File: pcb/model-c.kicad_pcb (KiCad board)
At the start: 2 copper layers, 82 x 144.9 mm, 115 parts, among them IC1 HTK16K33, IC2 HTK16K33, J1 Batt, J2 Conn_01x02_Socket, SW1 SW_SPST, SW10 SW_SPST, SW11 SW_SPST, SW12 SW_SPST, SW13 SW_SPST, SW14 SW_SPST, SW15 SW_SPST, SW16 SW_SPST, SW17 SW_SPST, SW18 SW_SPST, SW19 SW_SPST, SW2 SW_SPST, SW20 SW_SPDT, SW3 SW_SPST, SW4 SW_SPST, SW5 SW_SPST, SW6 SW_SPST, SW7 SW_SPST, SW8 SW_SPST, SW9 SW_SPST, U1 W25Q16JVUXIQ, U2 14seg, U3 RP2040, U4 MCP73831-2-OT, U5 XC9140, U6 14seg, Y1 12MHz

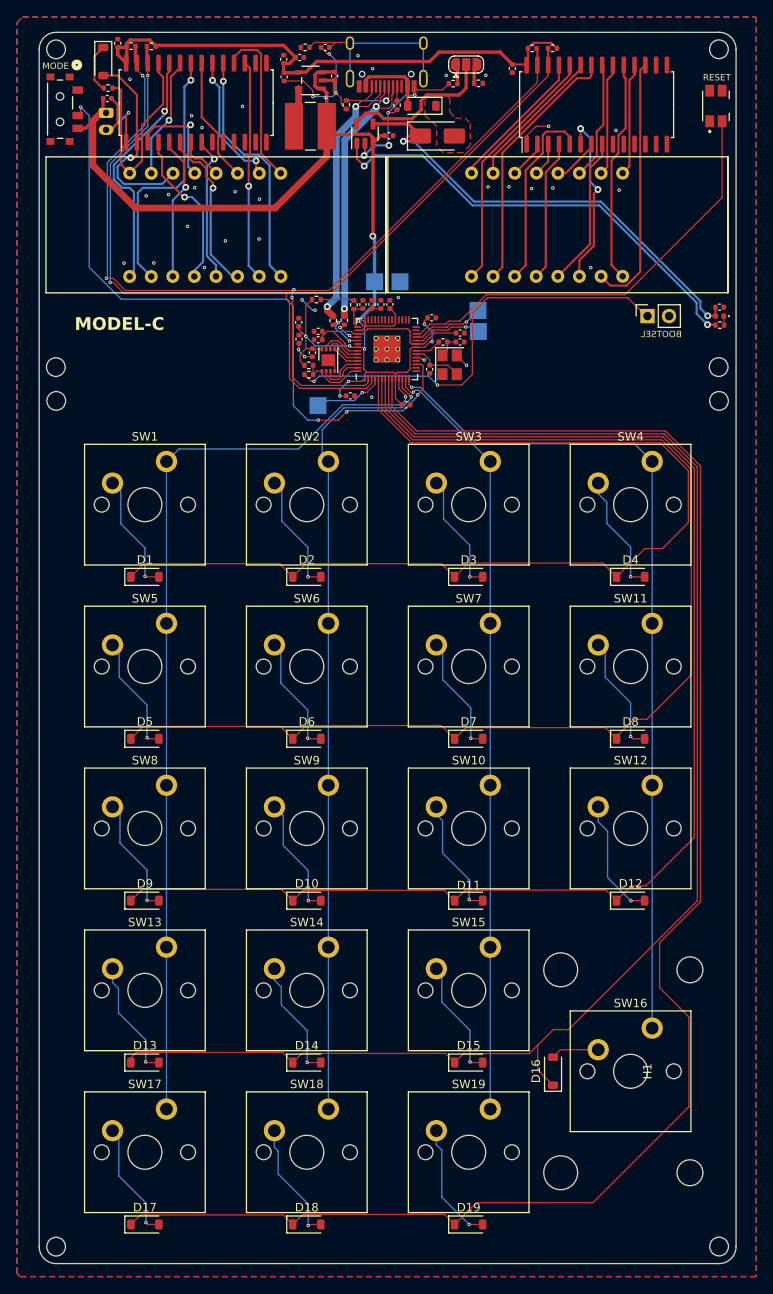
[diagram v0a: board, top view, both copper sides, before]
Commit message: fixed power switch, mode button, updated readme, panelized, and added much better styling
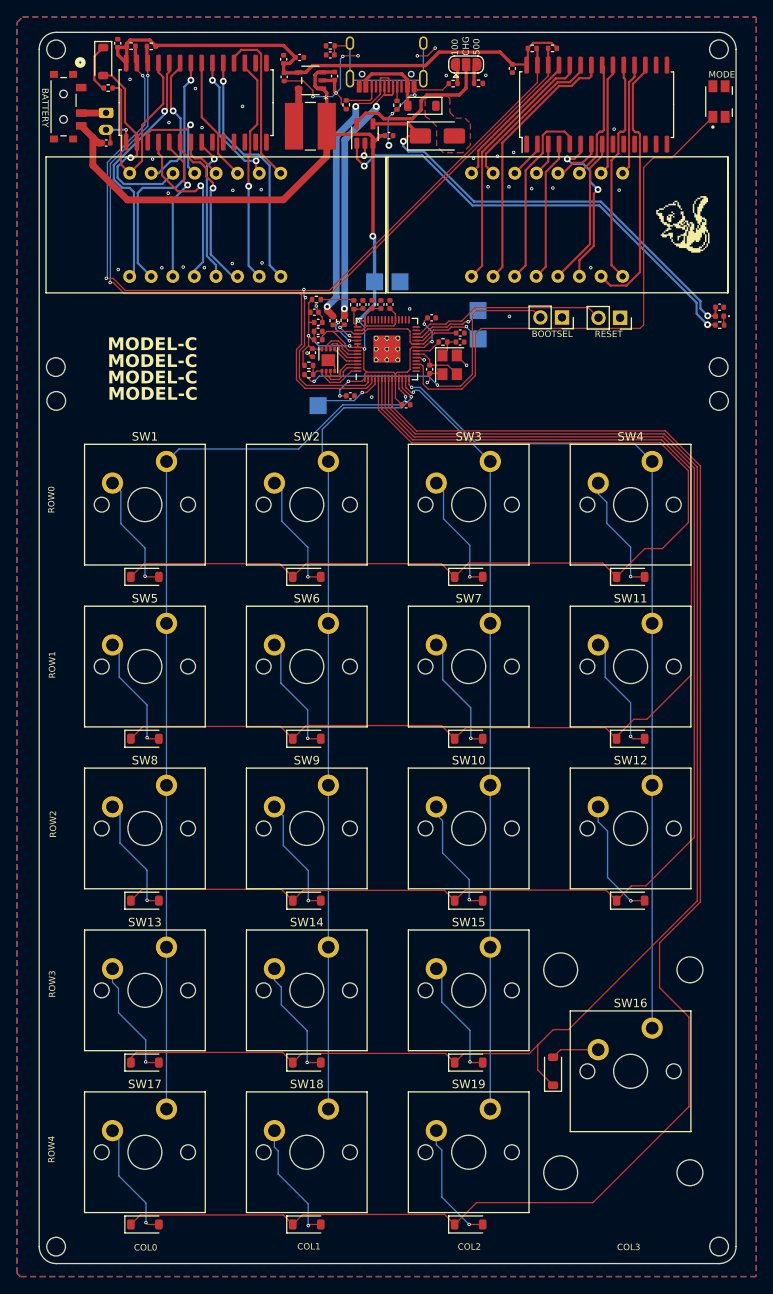
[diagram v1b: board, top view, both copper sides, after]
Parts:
- removed S2: RESET, EVQ-P7A01P:SW_EVQ-P7A01P
- removed SW20: SW_SPDT, footprints:MK-12C02-G020_GSW
- added G***: LOGO, LOGO, F.Cu at (121.6, 47.3)
- added G***: LOGO, LOGO, B.Cu at (86.8, 61.9)
- added J3: Conn_01x02_Socket, Connector_PinSocket_2.54mm:PinSocket_1x02_P2.54mm_Vertical, F.Cu at (114.2, 58.2)
- added S1: MODE, EVQ-P7A01P:SW_EVQ-P7A01P, F.Cu at (125.8, 32.8)
- added SW21: SW_SPDT, footprints:MK-12C02-G020_GSW, F.Cu at (48.7, 33.4)
- moved J2 10.1 mm to (107.4, 58.2), turned to -90 degrees
- moved C20 5.25 mm to (53.7, 37.7)
- moved C15 3.65 mm to (78.2, 57.6), turned to 0 degrees
- moved R8 2.97 mm to (80.1, 26.2)
- moved C14 2.30 mm to (78.7, 58.8), turned to 0 degrees
- moved C6 1.06 mm to (80.1, 27.3)
- moved TP1 0.87 mm to (97.5, 60.7)
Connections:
- J1 pad 1: +3V3 -> Net-(J1-Pin_1)
- J2 pad 1: /USB_BOOT -> GND
- J2 pad 2: GND -> /USB_BOOT
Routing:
- net /RUN: track 51.6 -> 23.2 mm
- net /mode: track 79.2 -> 64.3 mm, vias 4 -> 0
- net /USB_BOOT: track 50.8 -> 36.9 mm
- net GND: track 63.9 -> 56.2 mm, vias 43 -> 46
- net +3V3: track 148.4 -> 141.4 mm
- net Net-(J1-Pin_1): track 0.00 -> 2.94 mm
- net /USB_DP: track 36.4 -> 33.7 mm, vias 3 -> 2
- net Net-(USB1-SHIELD): track 23.0 -> 20.3 mm
- net Net-(IC2-COM2/KS1): track 19.0 -> 20.9 mm
- net Net-(IC2-ROW2/A0): track 14.4 -> 16.3 mm
- net Net-(IC1-ROW2/A0): track 17.0 -> 18.5 mm
- net /USB_DN: track 33.3 -> 31.8 mm
- net Net-(IC1-COM4): track 21.0 -> 19.9 mm
- net Net-(IC1-ROW8/K6): track 30.3 -> 31.2 mm
- net Net-(IC2-ROW8/K6): track 25.9 -> 26.7 mm
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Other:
- board text added: "+3V3"
- board text added: "100"
- board text added: "400mAh LiPo"
- board text added: "500"
- board text added: "8x 14 Segment Displays"
- board text added: "BATTERY"
- board text added: "CHG"
- board text added: "COL0"
- board text added: "COL1"
- board text added: "COL2"
- board text added: "COL3"
- board text added: "GND"
- board text added: "GPIO2"
- board text added: "MODEL-C V2.0"
- board text added: "Model-C - V2.0 Brian Hill 2025 github.com/TrojanPinata/Model-C"
- board text added: "ROW0"
- board text added: "ROW1"
- board text added: "ROW2"
- board text added: "ROW3"
- board text added: "ROW4"
- board text added: "RP2040"
- board text added: "SWCLK"
- board text added: "SWD"
